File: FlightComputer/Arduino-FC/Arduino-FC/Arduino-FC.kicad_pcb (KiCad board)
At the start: 2 copper layers, 95 x 86.9 mm, 32 parts, among them J1 Conn_01x04, J2 Conn_01x08, J3 Conn_01x06, J4 Conn_01x03, J5 Screw_Terminal_01x02, J6 Conn_01x02, J7 Conn_01x02, U1 NRF24L01_Breakout

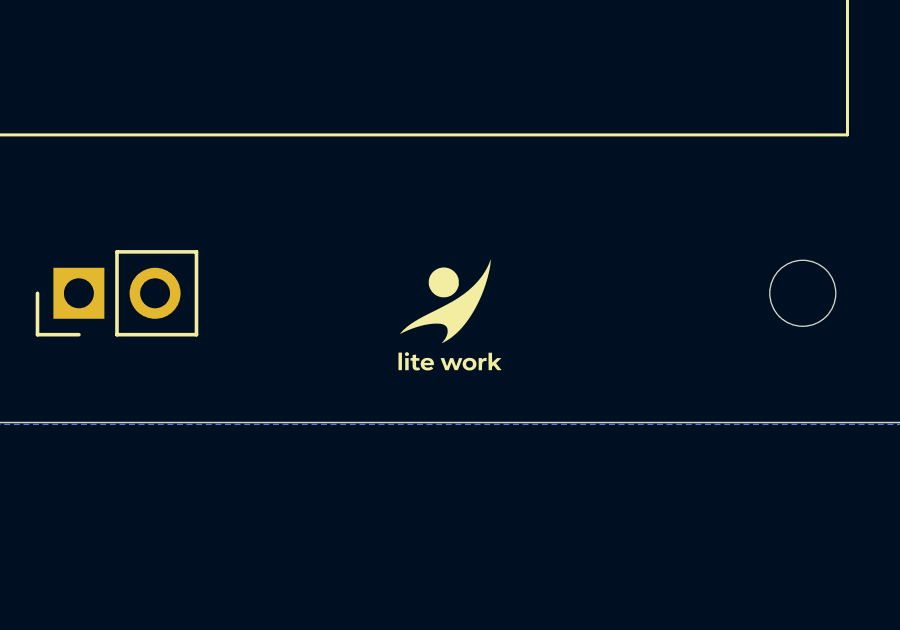
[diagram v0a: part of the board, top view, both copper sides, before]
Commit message: Revert second logo
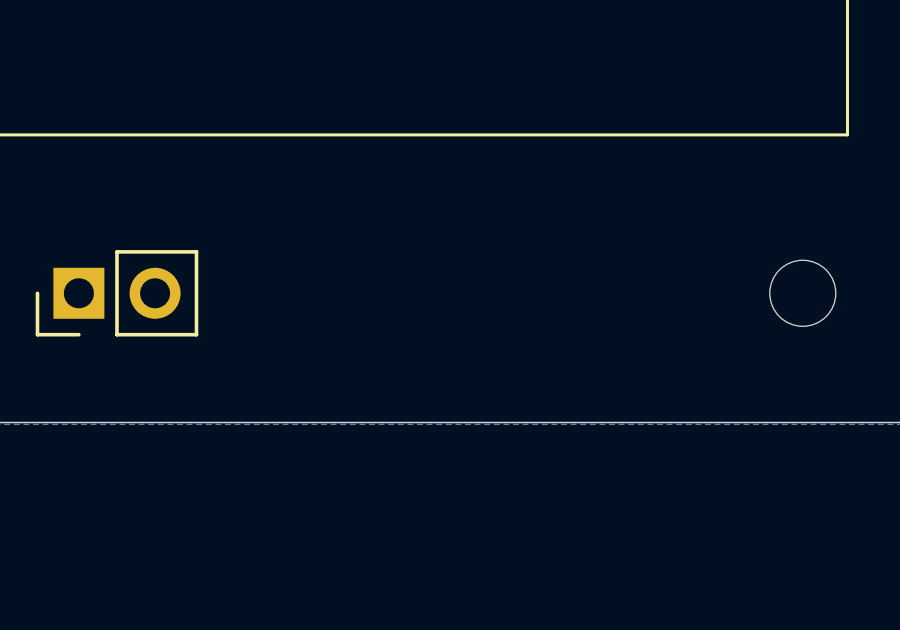
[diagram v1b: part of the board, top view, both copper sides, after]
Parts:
- removed the G*** at (189.0, 126.5)
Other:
- board text removed: "Designed By: Fawaaz Kamali Siddiqui"
- board text removed: "GitHub: https://github.com/fawaaz-kamali/CANSAT-LiteWork-2026"
- board text removed: "STEC Initiative 2026 (TMU CanSat) Team 'lite Work Fawaaz Kamali Siddiqui Hamid Karimi Mohammad Alwattar Ben Reboks Basim Allawala"

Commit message: Revert "Major Layout + Logo"
This reverts commit 6804596b28cb7cea65c62195238a1a9f434acbb5.
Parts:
- removed G***: LOGO, Logo:Logo
- moved R6 17.0 mm to (141.0, 124.5), turned to 0 degrees
- moved R5 16.6 mm to (141.0, 116.8), turned to 0 degrees
- moved R7 15.3 mm to (177.8, 71.1), turned to 90 degrees
- moved D1 12.8 mm to (165.1, 114.3), turned to -90 degrees
- moved R4 12.6 mm to (139.1, 45.7)
- moved C1 12.5 mm to (151.1, 52.3), turned to -90 degrees
- moved C2 11.3 mm to (152.4, 48.3), turned to 0 degrees
- moved R3 10.8 mm to (142.6, 45.7), turned to 0 degrees
- moved D2 8.42 mm to (165.1, 124.5), turned to -90 degrees
- moved J6 7.17 mm to (132.1, 54.6)
- moved R1 6.91 mm to (149.2, 54.0), turned to 90 degrees
- moved C3 6.88 mm to (147.3, 54.0), turned to -90 degrees
- moved R2 5.95 mm to (146.1, 54.0), turned to -90 degrees
- moved C5 5.56 mm to (142.9, 49.9), turned to -90 degrees
- moved J4 5.35 mm to (165.1, 53.3), turned to -90 degrees
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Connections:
- A1 pad 2: +5V -> unconnected-(A1-IOREF-Pad2)
- C4 pad 1: +5V -> Net-(VR1-VOUT)
- C5 pad 1: +5V -> Net-(VR1-VOUT)
- R3 pad 1: +5V -> Net-(VR1-VOUT)
- VR1 pad 3: +5V -> Net-(VR1-VOUT)
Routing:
- net +3V3: track 159.9 -> 0.00 mm
- net +5V: track 139.0 -> 0.00 mm
- net /BMP_SDA: track 60.3 -> 0.00 mm
- net /BMP_SCL: track 49.4 -> 0.00 mm, vias 2 -> 0
- net /NRF_CE: track 42.2 -> 0.00 mm, vias 2 -> 0
- net /NRF_CSN: track 36.9 -> 0.00 mm, vias 2 -> 0
- net /NRF_MOSI: track 32.7 -> 0.00 mm, vias 2 -> 0
- net Net-(A1-D6): track 28.8 -> 0.00 mm
- net /NRF_SCK: track 27.7 -> 0.00 mm
- net /NRF_MISO: track 24.0 -> 0.00 mm
- net /GPS_TX: track 19.7 -> 0.00 mm
- net /GPS_RX: track 16.8 -> 0.00 mm
- net Net-(A1-D5): track 16.8 -> 0.00 mm
- net Net-(D2-K): track 14.2 -> 0.00 mm
- net Net-(D1-K): track 14.2 -> 0.00 mm
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- removed copper zone on B.Cu, net GND
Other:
- board text removed: "(symbol "LOGO" (pin_names (offset 1.016)) (in_bom yes) (on_board yes) (property "Reference" "#G" (at 0 3.36525 0) (effects (font (size 1.27 1.27)) hide) ) (property "Value" "LOGO" (at 0 -3.36525 0) (effects (font (size 1.27 1.27)) hide) ) (property "Footprint" "" (at 0 0 0) (effects (font (size 1.27 1.27)) hide) ) (property "Datasheet" "" (at 0 0 0) (effects (font (size 1.27 1.27)) hide) ) (symbo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"
- board text removed: "+"
- board text removed: "ARM"
- board text removed: "POWER"
- board text removed: "SAFE"
- board text removed: "SERVO"
- board text removed: "SWITCH"

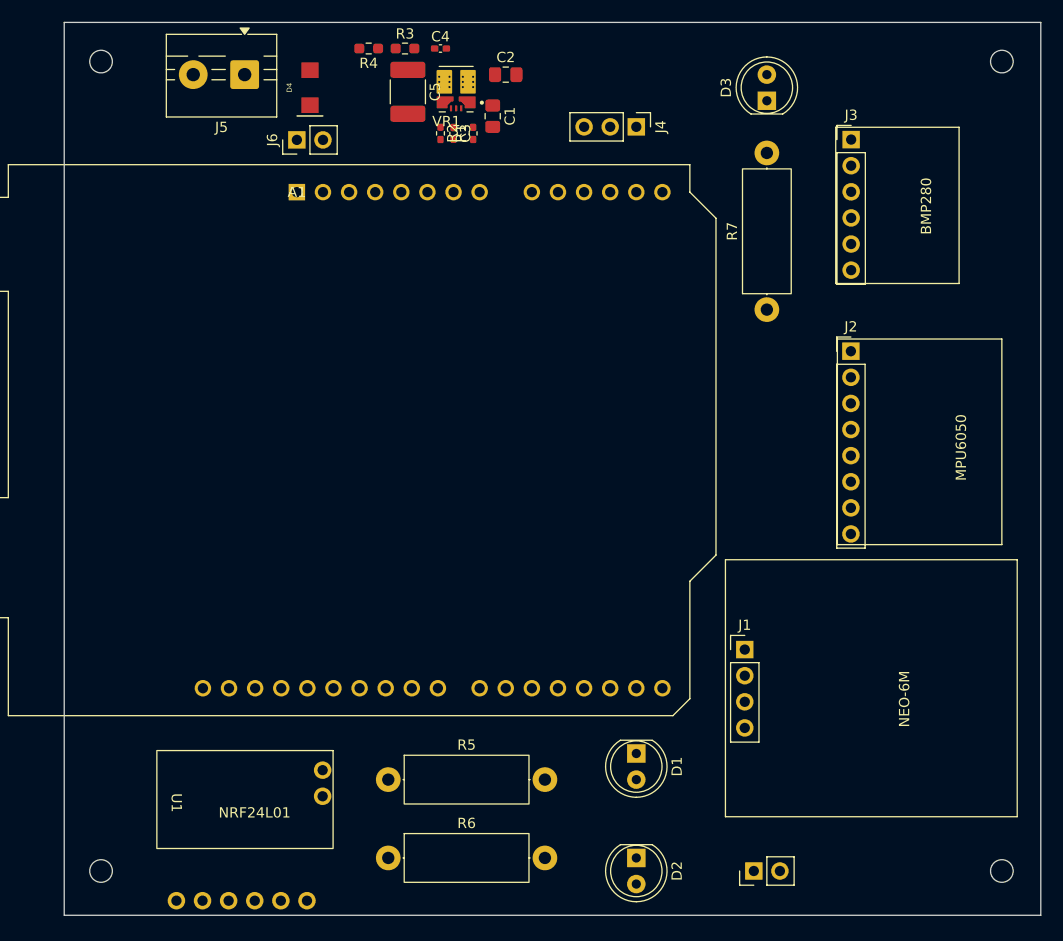
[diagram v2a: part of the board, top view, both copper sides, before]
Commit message: Bottom Routing Complete
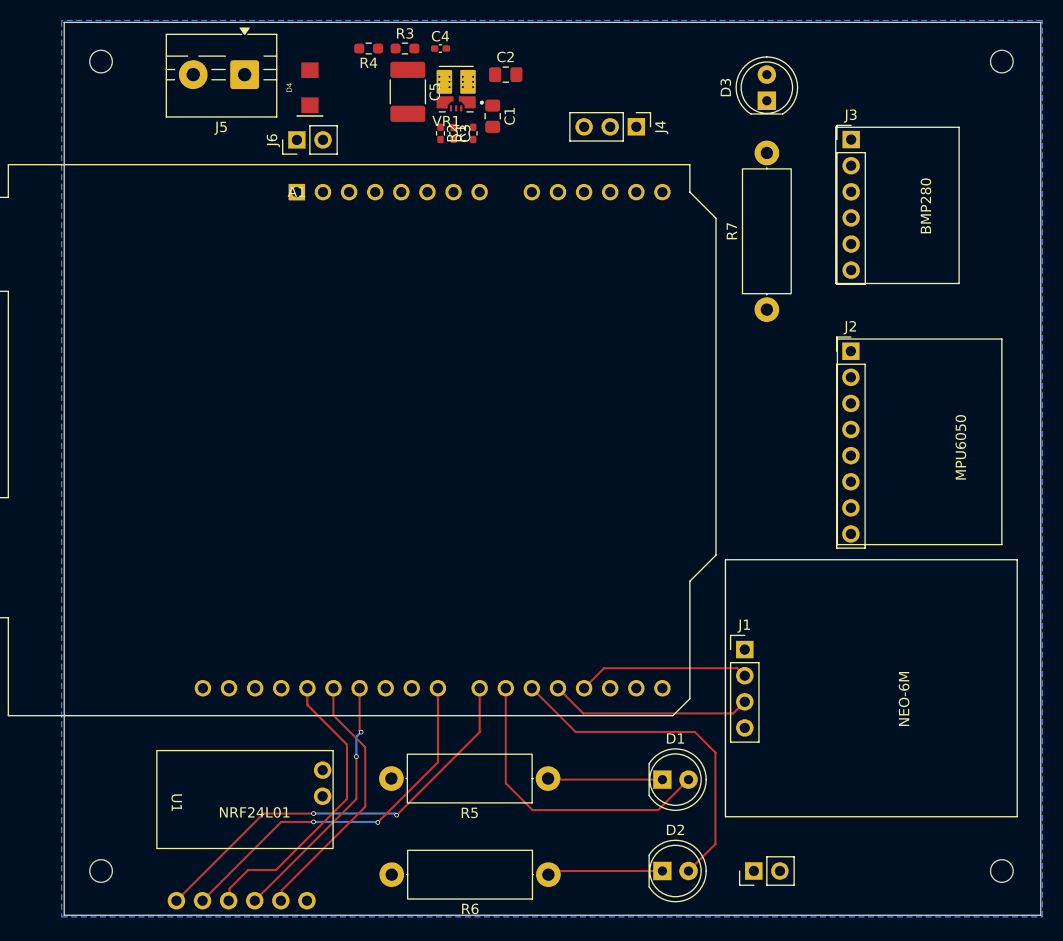
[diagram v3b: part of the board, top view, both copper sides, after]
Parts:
- moved R6 15.7 mm to (156.5, 126.1), turned to 180 degrees
- moved R5 15.5 mm to (156.5, 116.7), turned to 180 degrees
- moved D1 3.59 mm to (167.6, 116.8), turned to 0 degrees
- moved D2 2.84 mm to (167.6, 125.7), turned to 0 degrees
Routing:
- net /NRF_CE: track 0.00 -> 40.7 mm, vias 0 -> 2
- net /NRF_CSN: track 0.00 -> 35.7 mm, vias 0 -> 2
- net Net-(A1-D5): track 0.00 -> 33.1 mm
- net Net-(A1-D6): track 0.00 -> 29.3 mm
- net /NRF_SCK: track 0.00 -> 28.6 mm
- net /NRF_MISO: track 0.00 -> 25.4 mm
- net /NRF_MOSI: track 0.00 -> 25.0 mm, vias 0 -> 2
- net /GPS_TX: track 0.00 -> 19.7 mm
- net /GPS_RX: track 0.00 -> 16.7 mm
- net Net-(D2-K): track 0.00 -> 11.2 mm
- net Net-(D1-K): track 0.00 -> 11.2 mm
- added copper zone on B.Cu, net GND

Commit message: MPU + BMP Routing
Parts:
- moved R7 14.7 mm to (177.8, 56.4), turned to -90 degrees
- moved J4 5.17 mm to (163.4, 48.5), turned to 0 degrees
- moved D4 4.89 mm to (133.8, 54.4), turned to 180 degrees
- moved J6 4.63 mm to (134.0, 50.4), turned to 180 degrees
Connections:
- A1 pad 12: unconnected-(A1-A3-Pad12) -> /SERVO
- A1 pad 2: unconnected-(A1-IOREF-Pad2) -> +5V
- A1 pad 24: /SERVO -> unconnected-(A1-D9-Pad24)
- C4 pad 1: Net-(VR1-VOUT) -> +5V
- C5 pad 1: Net-(VR1-VOUT) -> +5V
- R3 pad 1: Net-(VR1-VOUT) -> +5V
- VR1 pad 3: Net-(VR1-VOUT) -> +5V
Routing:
- net +3V3: track 0.00 -> 110.7 mm
- net +5V: track 0.00 -> 81.2 mm
- net /BMP_SDA: track 0.00 -> 57.9 mm
- net /BMP_SCL: track 0.00 -> 51.0 mm, vias 0 -> 2
- net Net-(D3-K): track 0.00 -> 5.60 mm

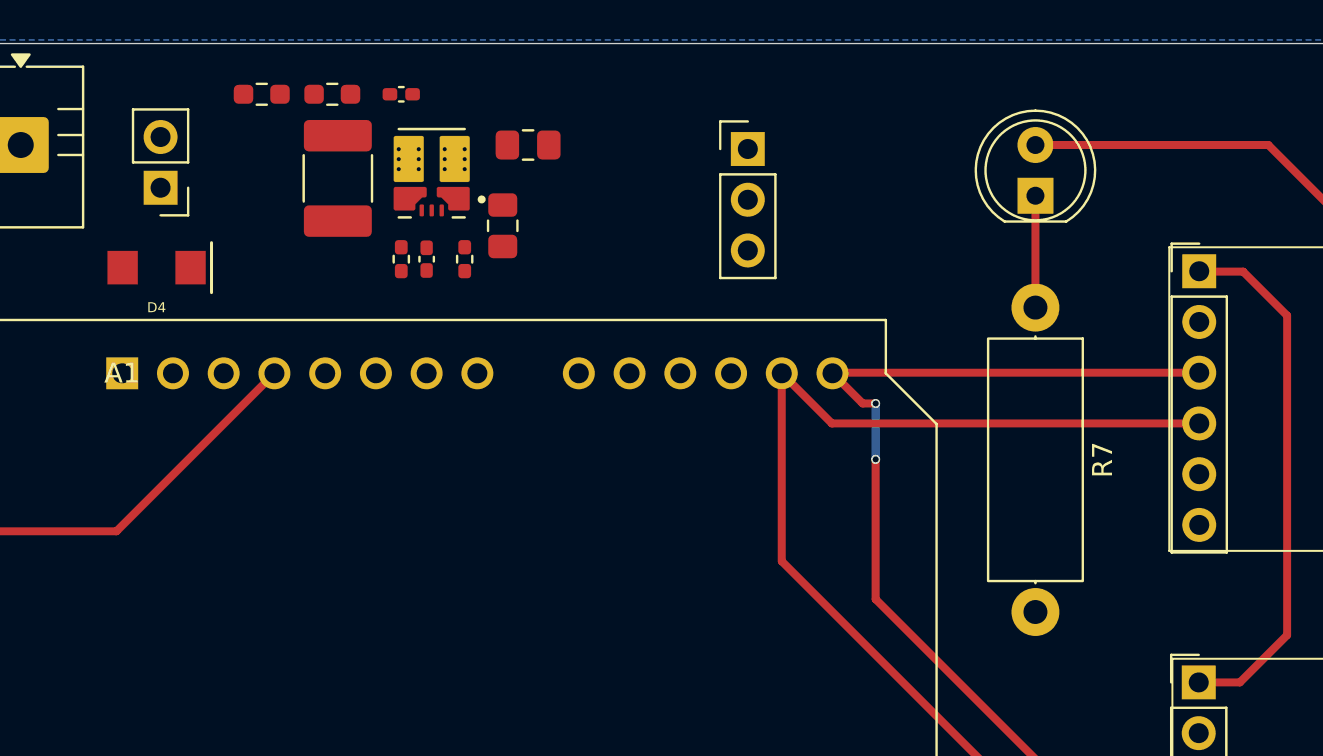
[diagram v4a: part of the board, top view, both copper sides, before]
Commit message: Buck Layout
Update buck footprint
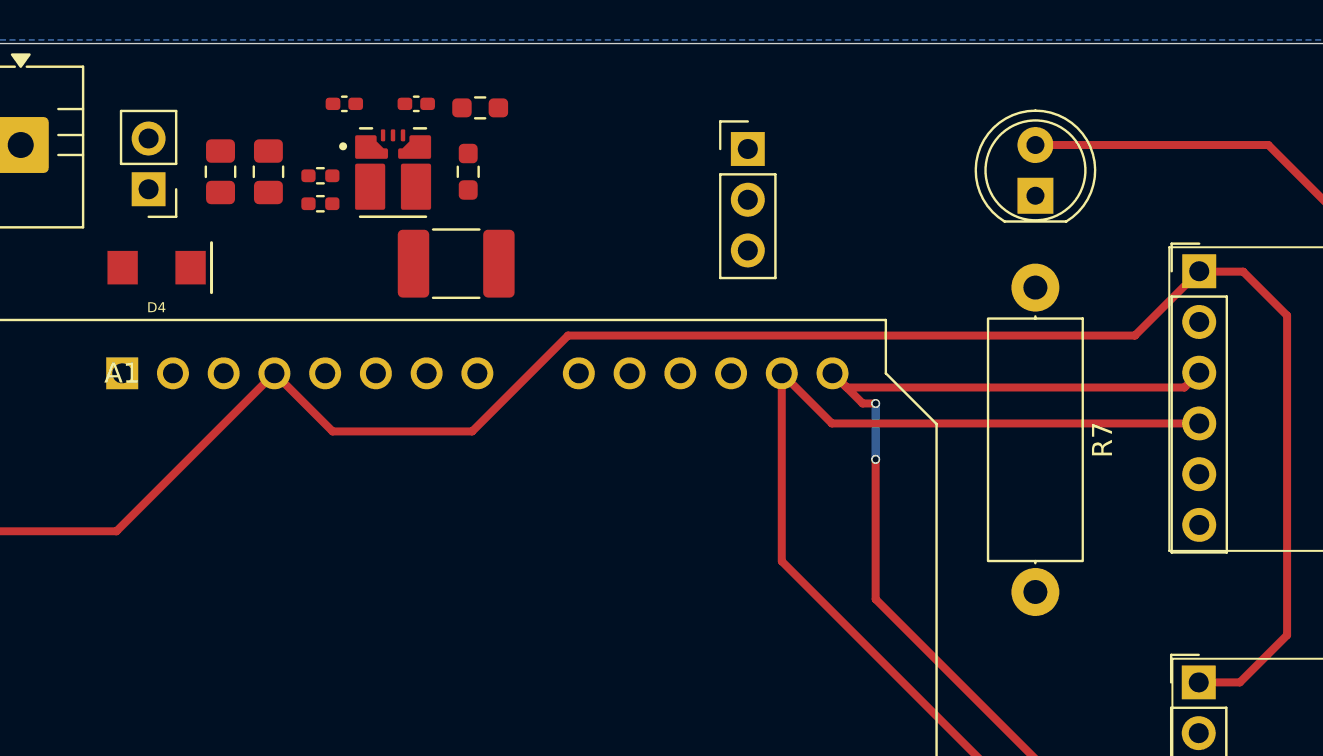
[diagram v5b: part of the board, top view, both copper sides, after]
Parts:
- moved C2 15.5 mm to (137.0, 49.6), turned to 90 degrees
- moved C1 12.0 mm to (139.4, 49.6), turned to 90 degrees
- moved R4 11.0 mm to (150.0, 46.4), turned to 0 degrees
- moved C3 8.80 mm to (143.2, 46.2), turned to 180 degrees
- moved R1 8.34 mm to (142.0, 49.8), turned to 180 degrees
- moved R3 7.83 mm to (149.4, 49.6), turned to 90 degrees
- moved C5 7.30 mm to (148.8, 54.2), turned to 0 degrees
- moved R2 4.91 mm to (142.0, 51.2), turned to 180 degrees
- moved VR1 1.94 mm to (145.6, 49.7), turned to 0 degrees
- moved R7 1.00 mm to (177.8, 55.4)
- moved C4 0.89 mm to (146.8, 46.2), turned to 180 degrees
- moved J6 0.60 mm to (133.4, 50.5)
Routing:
- net +3V3: track 110.7 -> 161.6 mm
- net Net-(D3-K): track 5.60 -> 0.00 mm
- net /BMP_SCL: track 51.0 -> 51.6 mm

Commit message: Complete Layout 1
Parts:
- moved R2 3.80 mm to (142.0, 47.4)
- moved C5 3.00 mm to (145.8, 54.2)
- moved R1 0.40 mm to (142.0, 49.4)
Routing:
- net +5V: track 81.2 -> 149.6 mm
- net Net-(J6-Pin_2): track 0.00 -> 10.7 mm
- net GND: track 0.00 -> 9.69 mm, vias 0 -> 6
- net Net-(VR1-FB): track 0.00 -> 8.85 mm
- net Net-(VR1-EN): track 0.00 -> 8.63 mm, vias 0 -> 2
- net VBAT+: track 0.00 -> 8.25 mm
- net /SERVO: track 0.00 -> 6.50 mm, vias 0 -> 1
- net Net-(D4-K): track 0.00 -> 4.79 mm
- net Net-(D3-K): track 0.00 -> 4.60 mm

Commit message: Warnings Resolution
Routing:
- net Net-(J6-Pin_2): track 10.7 -> 13.1 mm
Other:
- board text added: "+"
- board text added: "ARM"
- board text added: "POWER"
- board text added: "SAFE"
- board text added: "SERVO"
- board text added: "SWITCH"
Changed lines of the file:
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@@
 				(font
 					(size 1 1)
-					(thickness 0.15)
+					(thickness 0.16)
 				)
 			)
@@
 			(at 0 -2 0)
 			(layer "F.SilkS")
+			(hide yes)
 			(effects
 				(font
@@
 			(at 1.27 -3.96 0)
 			(layer "F.SilkS")
+			(hide yes)
 			(effects
 				(font
@@
 		(tags "Resistor Axial_DIN0414 series Axial Horizontal pin pitch 15.24mm 2W length 11.9mm diameter 4.5mm")
 		(property "Reference" "R5"
-			(at 7.62 -3.37 0)
+			(at 7.51507 3.338401 0)
 			(layer "F.SilkS")
 			(effects
 				(font
 					(size 1 1)
-					(thickness 0.15)
+					(thickness 0.16)
 				)
 			)
 		)
 		(property "Value" "470"
-			(at 7.62 3.37 0)
+			(at 7.5148 -3.4616 0)
 			(layer "F.Fab")
 			(effects
@@
 		(tags "Resistor Axial_DIN0414 series Axial Horizontal pin pitch 15.24mm 2W length 11.9mm diameter 4.5mm")
 		(property "Reference" "R6"
-			(at 7.62 -3.37 0)
+			(at 7.547944 3.285019 0)
 			(layer "F.SilkS")
 			(effects
 				(font
 					(size 1 1)
-					(thickness 0.15)
+					(thickness 0.16)
 				)
 			)
 		)
 		(property "Value" "470"
-			(at 7.62 3.37 0)
+			(at 7.747944 -3.314981 0)
 			(layer "F.Fab")
 			(effects
@@
 			(at 1.27 -3.96 0)
 			(layer "F.SilkS")
+			(hide yes)
 			(effects
 				(font
@@
 			(at 0 0 180)
 			(layer "F.SilkS")
+			(hide yes)
 			(effects
 				(font
@@
 		(layer "F.SilkS")
 	)
+	(gr_line
+		(start 162.8 121.3)
+		(end 172.8 121.3)
+		(stroke
+			(width 0.1)
+			(type default)
+		)
+		(layer "F.SilkS")
+	)
+	(gr_rect
+		(start 173 44.4)
+		(end 182.6 53.6)
+		(stroke
+			(width 0.1)
+			(type default)
+		)
+		(fill no)
+		(layer "F.SilkS")
+	)
+	(gr_rect
+		(start 162.8 113.2)
+		(end 172.8 129.4)
+		(stroke
+			(width 0.1)
+			(type default)
+		)
+		(fill no)
+		(layer "F.SilkS")
+	)
 	(gr_rect
 		(start 173.77 95.45)
@@
 		(layer "F.Fab")
 	)
+	(gr_text "SERVO\n"
+		(at 161 46.2 0)
+		(layer "F.SilkS")
+		(effects
+			(font
+				(size 1 1)
+				(thickness 0.16)
+			)
+			(justify left bottom)
+		)
+	)
+	(gr_text "SWITCH"
+		(at 130.6 45.8 0)
+		(layer "F.SilkS")
+		(effects
+			(font
+				(size 1 1)
+				(thickness 0.16)
+			)
+			(justify left bottom)
+		)
+	)
 	(gr_text "NEO-6M\n"
 		(at 201.2 111.2 90)
@@
 			(font
 				(size 1 1)
-				(thickness 0.1)
+				(thickness 0.16)
+			)
+			(justify left bottom)
+		)
+	)
+	(gr_text "SAFE"
+		(at 165.2 127.6 90)
+		(layer "F.SilkS")
+		(effects
+			(font
+				(size 1 1)
+				(thickness 0.16)
 			)
 			(justify left bottom)
@@
 			(font
 				(size 1 1)
-				(thickness 0.1)
+				(thickness 0.16)
+			)
+			(justify left bottom)
+		)
+	)
+	(gr_text "POWER\n"
+		(at 175.2 46 0)
+		(layer "F.SilkS")
+		(effects
+			(font
+				(size 1 1)
+				(thickness 0.16)
 			)
 			(justify left bottom)
@@
 			(font
 				(size 1 1)
-				(thickness 0.1)
+				(thickness 0.16)
 			)
 			(justify left bottom)
@@
 			(font
 				(size 1 1)
-				(thickness 0.1)
+				(thickness 0.16)
+			)
+			(justify left bottom)
+		)
+	)
+	(gr_text "ARM\n"
+		(at 165.2 118.4 90)
+		(layer "F.SilkS")
+		(effects
+			(font
+				(size 1 1)
+				(thickness 0.16)
+			)
+			(justify left bottom)
+		)
+	)
+	(gr_text "+"
+		(at 127.8 54 0)
+		(layer "F.SilkS")
+		(effects
+			(font
+				(size 1 1)
+				(thickness 0.16)
 			)
 			(justify left bottom)
@@
 		(width 0.6)
 		(layer "F.Cu")
+		(net 40)
+	)
+	(segment
+		(start 137 50.6375)
+		(end 139.4 50.6375)
+		(width 0.6)
+		(layer "F.Cu")
